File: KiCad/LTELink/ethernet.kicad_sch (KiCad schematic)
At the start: 68 parts, among them IC1 RTL8305NB-VC-CG, J15 Conn_01x04, J22 Conn_01x04, J23 Conn_01x04, J24 Conn_01x04, Y2 X322525MOB4SI

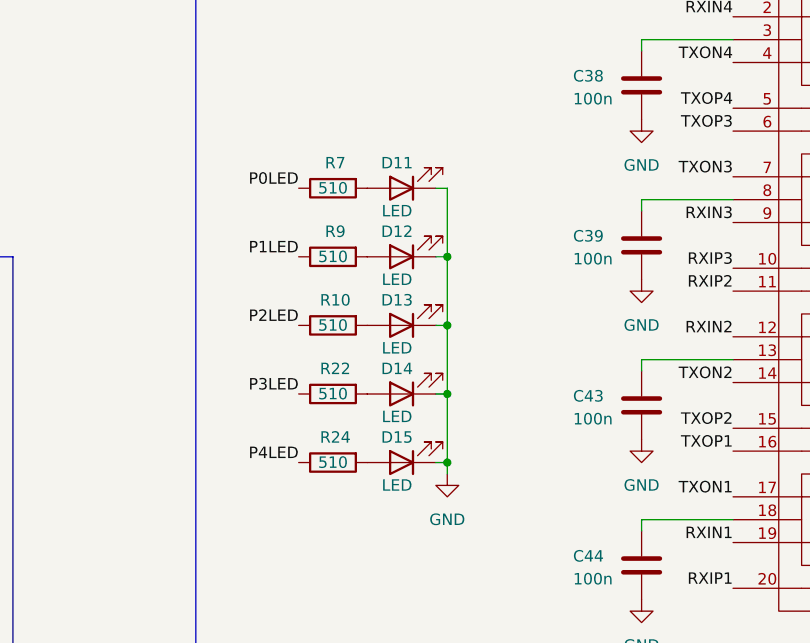
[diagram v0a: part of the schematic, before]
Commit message: Moved LEDs to other side of the board, which means they mustbe assembled by hand. Added UART 5 test points.
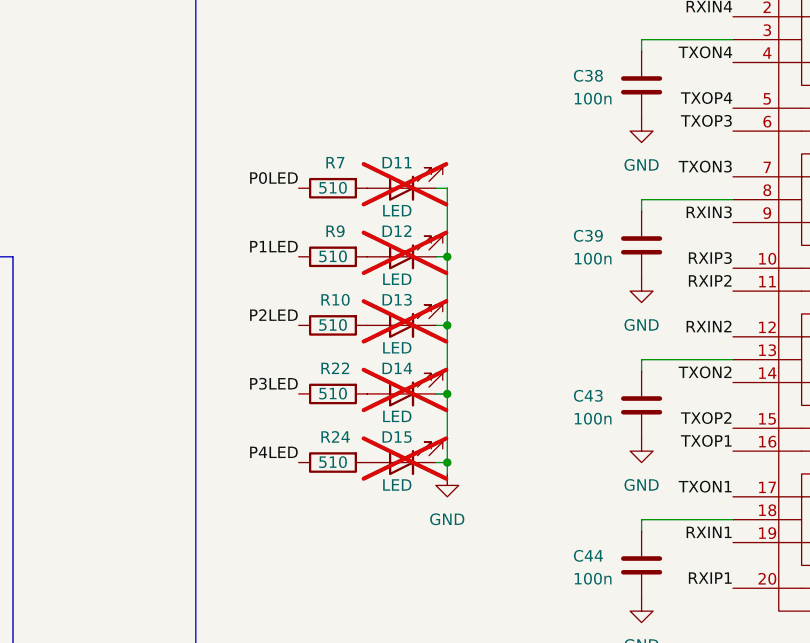
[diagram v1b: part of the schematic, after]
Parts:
- D11, D12, D13, D14, D15: footprint LED_SMD:LED_0805_2012Metric -> LED_SMD:LED_0805_2012Metric_Pad1.15x1.40mm_HandSolder; now not fitted
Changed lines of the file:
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@@
 		(on_board yes)
 		(in_pos_files yes)
-		(dnp no)
+		(dnp yes)
 		(property "Reference" "D11"
 			(at 261.112 73.406 0)
@@
 			)
 		)
-		(property "Footprint" "LED_SMD:LED_0805_2012Metric"
+		(property "Footprint" "LED_SMD:LED_0805_2012Metric_Pad1.15x1.40mm_HandSolder"
 			(at 261.62 76.2 0)
 			(hide yes)
@@
 		(on_board yes)
 		(in_pos_files yes)
-		(dnp no)
+		(dnp yes)
 		(property "Reference" "D15"
 			(at 261.112 103.886 0)
@@
 			)
 		)
-		(property "Footprint" "LED_SMD:LED_0805_2012Metric"
+		(property "Footprint" "LED_SMD:LED_0805_2012Metric_Pad1.15x1.40mm_HandSolder"
 			(at 261.62 106.68 0)
 			(hide yes)
@@
 		(on_board yes)
 		(in_pos_files yes)
-		(dnp no)
+		(dnp yes)
 		(property "Reference" "D12"
 			(at 261.112 81.026 0)
@@
 			)
 		)
-		(property "Footprint" "LED_SMD:LED_0805_2012Metric"
+		(property "Footprint" "LED_SMD:LED_0805_2012Metric_Pad1.15x1.40mm_HandSolder"
 			(at 261.62 83.82 0)
 			(hide yes)
@@
 		(on_board yes)
 		(in_pos_files yes)
-		(dnp no)
+		(dnp yes)
 		(property "Reference" "D14"
 			(at 261.112 96.266 0)
@@
 			)
 		)
-		(property "Footprint" "LED_SMD:LED_0805_2012Metric"
+		(property "Footprint" "LED_SMD:LED_0805_2012Metric_Pad1.15x1.40mm_HandSolder"
 			(at 261.62 99.06 0)
 			(hide yes)
@@
 		(on_board yes)
 		(in_pos_files yes)
-		(dnp no)
+		(dnp yes)
 		(property "Reference" "D13"
 			(at 261.112 88.646 0)
@@
 			)
 		)
-		(property "Footprint" "LED_SMD:LED_0805_2012Metric"
+		(property "Footprint" "LED_SMD:LED_0805_2012Metric_Pad1.15x1.40mm_HandSolder"
 			(at 261.62 91.44 0)
 			(hide yes)

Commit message: Finalize LTELink V2 for production
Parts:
- C14, C15, C32, C34: footprint Capacitor_SMD:C_0402_1005Metric -> Capacitor_SMD:C_0603_1608Metric_Pad1.08x0.95mm_HandSolder; now not fitted
- L1: LCSC Part # (none) -> H4001CG; LCSC Part Name H4001CG -> (none); Supplier Part C2904733 -> (none)
- R20, R21, R23, R8: footprint Resistor_SMD:R_0402_1005Metric -> Resistor_SMD:R_0603_1608Metric; LCSC Part # (none) -> C4275
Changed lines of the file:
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@@
 		(on_board yes)
 		(in_pos_files yes)
-		(dnp no)
+		(dnp yes)
 		(property "Reference" "C34"
 			(at 346.71 116.84 90)
@@
 			)
 		)
-		(property "Footprint" "Capacitor_SMD:C_0402_1005Metric"
+		(property "Footprint" "Capacitor_SMD:C_0603_1608Metric_Pad1.08x0.95mm_HandSolder"
 			(at 350.52 112.0648 0)
 			(hide yes)
@@
 			)
 		)
-		(property "Footprint" "Resistor_SMD:R_0402_1005Metric"
+		(property "Footprint" "Resistor_SMD:R_0603_1608Metric"
 			(at 336.55 61.468 90)
 			(hide yes)
@@
 			)
 		)
+		(property "LCSC Part #" "C4275"
+			(at 336.55 59.69 90)
+			(hide yes)
+			(show_name no)
+			(do_not_autoplace no)
+			(effects
+				(font
+					(size 1.27 1.27)
+				)
+			)
+		)
 		(pin "2"
 		)
@@
 			)
 		)
-		(property "Footprint" "Resistor_SMD:R_0402_1005Metric"
+		(property "Footprint" "Resistor_SMD:R_0603_1608Metric"
 			(at 336.55 79.248 90)
 			(hide yes)
@@
 			)
 		)
+		(property "LCSC Part #" "C4275"
+			(at 336.55 77.47 90)
+			(hide yes)
+			(show_name no)
+			(do_not_autoplace no)
+			(effects
+				(font
+					(size 1.27 1.27)
+				)
+			)
+		)
 		(pin "2"
 		)
@@
 			)
 		)
-		(property "Footprint" "Resistor_SMD:R_0402_1005Metric"
+		(property "Footprint" "Resistor_SMD:R_0603_1608Metric"
 			(at 336.55 114.808 90)
 			(hide yes)
@@
 			)
 		)
+		(property "LCSC Part #" "C4275"
+			(at 336.55 113.03 90)
+			(hide yes)
+			(show_name no)
+			(do_not_autoplace no)
+			(effects
+				(font
+					(size 1.27 1.27)
+				)
+			)
+		)
 		(pin "2"
 		)
@@
 		(on_board yes)
 		(in_pos_files yes)
-		(dnp no)
+		(dnp yes)
 		(property "Reference" "C15"
 			(at 346.71 81.28 90)
@@
 			)
 		)
-		(property "Footprint" "Capacitor_SMD:C_0402_1005Metric"
+		(property "Footprint" "Capacitor_SMD:C_0603_1608Metric_Pad1.08x0.95mm_HandSolder"
 			(at 350.52 76.5048 0)
 			(hide yes)
@@
 			)
 		)
-		(property "Footprint" "Resistor_SMD:R_0402_1005Metric"
+		(property "Footprint" "Resistor_SMD:R_0603_1608Metric"
 			(at 336.55 97.028 90)
 			(hide yes)
@@
 			)
 		)
+		(property "LCSC Part #" "C4275"
+			(at 336.55 95.25 90)
+			(hide yes)
+			(show_name no)
+			(do_not_autoplace no)
+			(effects
+				(font
+					(size 1.27 1.27)
+				)
+			)
+		)
 		(pin "2"
 		)
@@
 		(on_board yes)
 		(in_pos_files yes)
-		(dnp no)
+		(dnp yes)
 		(property "Reference" "C32"
 			(at 346.71 99.06 90)
@@
 			)
 		)
-		(property "Footprint" "Capacitor_SMD:C_0402_1005Metric"
+		(property "Footprint" "Capacitor_SMD:C_0603_1608Metric_Pad1.08x0.95mm_HandSolder"
 			(at 350.52 94.2848 0)
 			(hide yes)
@@
 			)
 		)
-		(property "Supplier Part" "C2904733"
-			(at 313.69 87.63 0)
-			(hide yes)
-			(show_name no)
-			(do_not_autoplace no)
-			(effects
-				(font
-					(size 1.27 1.27)
-				)
-			)
-		)
 		(property "Supplier" "LCSC"
 			(at 313.69 87.63 0)
@@
 			)
 		)
-		(property "LCSC Part Name" "H4001CG"
+		(property "LCSC Part #" "H4001CG"
 			(at 313.69 87.63 0)
 			(hide yes)
@@
 		(on_board yes)
 		(in_pos_files yes)
-		(dnp no)
+		(dnp yes)
 		(property "Reference" "C14"
 			(at 346.71 63.5 90)
@@
 			)
 		)
-		(property "Footprint" "Capacitor_SMD:C_0402_1005Metric"
+		(property "Footprint" "Capacitor_SMD:C_0603_1608Metric_Pad1.08x0.95mm_HandSolder"
 			(at 350.52 58.7248 0)
 			(hide yes)
